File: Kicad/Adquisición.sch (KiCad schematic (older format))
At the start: 28 parts, among them U2 TLC2274, U3 TLC2274

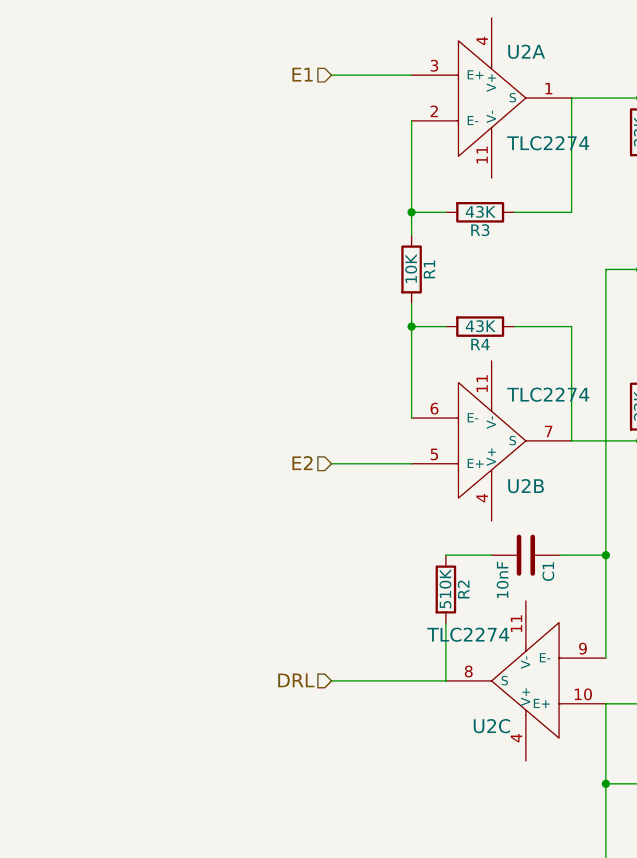
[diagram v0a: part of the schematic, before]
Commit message: Agregados footprints de pin headers para elementos faltantes (falta USB)
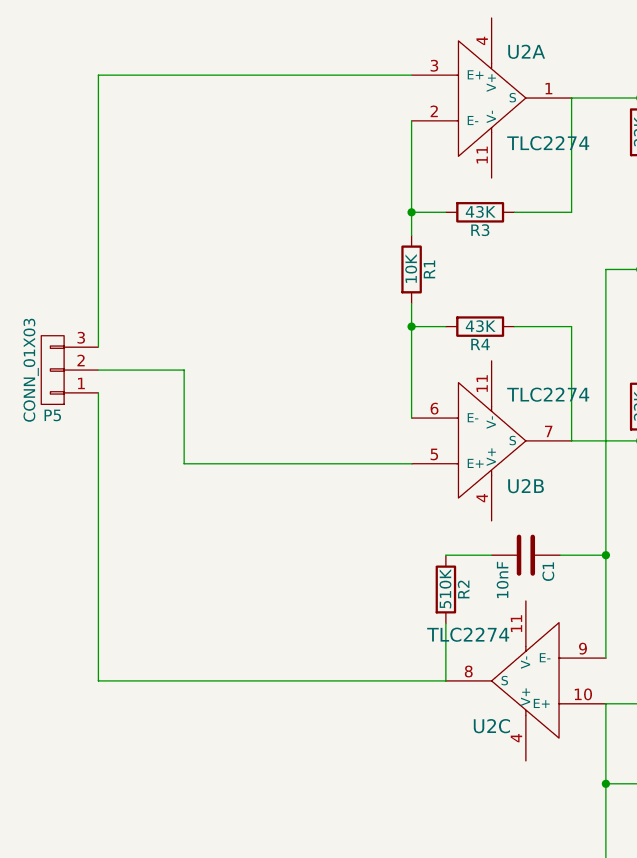
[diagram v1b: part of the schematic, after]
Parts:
- added P5: CONN_01X03, EMG:Pin_Header_Straight_1x03_Pitch2.54mm, symbol CONN_01X03
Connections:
- net DRL: no longer names the net of R2.2, U2.8 (S)
- net DRL: now also P5.1 (P1)
- net E1: no longer names the net of U2.3 (E+)
- net E1: now also P5.3 (P3)
- net E2: no longer names the net of U2.5 (E+)
- net E2: now also P5.2 (P2)
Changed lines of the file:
@@
 $EndComp
 $Comp
-L VCC #PWR1
+L VCC #PWR01
 U 1 1 57DD6A08
 P 4550 5200
-F 0 "#PWR1" H 4550 5050 50  0001 C CNN
+F 0 "#PWR01" H 4550 5050 50  0001 C CNN
 F 1 "VCC" H 4550 5350 50  0000 C CNN
 F 2 "" H 4550 5200 50  0000 C CNN
@@
 $EndComp
 $Comp
-L GND #PWR2
+L GND #PWR02
 U 1 1 57DD6A0E
 P 4550 5900
-F 0 "#PWR2" H 4550 5650 50  0001 C CNN
+F 0 "#PWR02" H 4550 5650 50  0001 C CNN
 F 1 "GND" H 4550 5750 50  0000 C CNN
 F 2 "" H 4550 5900 50  0000 C CNN
@@
 $EndComp
 $Comp
-L GND #PWR7
+L GND #PWR03
 U 1 1 57DD6A14
 P 5750 3700
-F 0 "#PWR7" H 5750 3450 50  0001 C CNN
+F 0 "#PWR03" H 5750 3450 50  0001 C CNN
 F 1 "GND" H 5750 3550 50  0000 C CNN
 F 2 "" H 5750 3700 50  0000 C CNN
@@
 $EndComp
 $Comp
-L VCC #PWR6
+L VCC #PWR04
 U 1 1 57DD6A1A
 P 5750 2800
-F 0 "#PWR6" H 5750 2650 50  0001 C CNN
+F 0 "#PWR04" H 5750 2650 50  0001 C CNN
 F 1 "VCC" H 5750 2950 50  0000 C CNN
 F 2 "" H 5750 2800 50  0000 C CNN
@@
 $EndComp
 $Comp
-L VCC #PWR4
+L VCC #PWR05
 U 1 1 57DD6A3A
 P 5250 5300
-F 0 "#PWR4" H 5250 5150 50  0001 C CNN
+F 0 "#PWR05" H 5250 5150 50  0001 C CNN
 F 1 "VCC" H 5250 5450 50  0000 C CNN
 F 2 "" H 5250 5300 50  0000 C CNN
@@
 $EndComp
 $Comp
-L GND #PWR5
+L GND #PWR06
 U 1 1 57DD6A40
 P 5250 5950
-F 0 "#PWR5" H 5250 5700 50  0001 C CNN
+F 0 "#PWR06" H 5250 5700 50  0001 C CNN
 F 1 "GND" H 5250 5800 50  0000 C CNN
 F 2 "" H 5250 5950 50  0000 C CNN
@@
 $EndComp
 $Comp
-L GND #PWR3
+L GND #PWR07
 U 1 1 57DD6A46
 P 5000 5950
-F 0 "#PWR3" H 5000 5700 50  0001 C CNN
+F 0 "#PWR07" H 5000 5700 50  0001 C CNN
 F 1 "GND" H 5000 5800 50  0000 C CNN
 F 2 "" H 5000 5950 50  0000 C CNN
@@
 Wire Wire Line
 	5250 5650 5250 5600
-Text HLabel 3000 1850 0    60   Input ~ 0
-E1
-Text HLabel 3000 3550 0    60   Input ~ 0
-E2
-Text HLabel 3000 4500 0    60   Input ~ 0
-DRL
-Wire Wire Line
-	3000 3550 3350 3550
-Wire Wire Line
-	3000 1850 3350 1850
 $Comp
 L R R20
@@
 $EndComp
 $Comp
-L GND #PWR8
+L GND #PWR08
 U 1 1 57DD7EDB
 P 8050 3550
-F 0 "#PWR8" H 8050 3300 50  0001 C CNN
+F 0 "#PWR08" H 8050 3300 50  0001 C CNN
 F 1 "GND" H 8050 3400 50  0000 C CNN
 F 2 "" H 8050 3550 50  0000 C CNN
@@
 Vout
 Connection ~ 8050 3250
+$Comp
+L CONN_01X03 P5
+U 1 1 58A72533
+P 1780 3140
+F 0 "P5" H 1780 3340 50  0000 C CNN
+F 1 "CONN_01X03" V 1880 3140 50  0000 C CNN
+F 2 "EMG:Pin_Header_Straight_1x03_Pitch2.54mm" H 1780 3140 50  0001 C CNN
+F 3 "" H 1780 3140 50  0000 C CNN
+	1    1780 3140
+	-1   0    0    1
+$EndComp
 Wire Wire Line
-	3000 4500 3500 4500
+	1980 3240 1980 4500
+Wire Wire Line
+	1980 4500 3500 4500
+Wire Wire Line
+	3350 3550 2355 3550
+Wire Wire Line
+	2355 3550 2355 3140
+Wire Wire Line
+	2355 3140 1980 3140
+Wire Wire Line
+	1980 3040 1980 1850
+Wire Wire Line
+	1980 1850 3350 1850
 $EndSCHEMATC

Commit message: Versión unificada
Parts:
- C1, C2, C3, C4, C5, C6: footprint EMG:C_0805 -> EMG:C_0603
- R1, R10, R11, R12, R13, R14, R15, R16, R17, R18, R19, R2, R20, R3, R4, R5, R6, R7, R8, R9: footprint EMG:R_0805 -> EMG:R_0603
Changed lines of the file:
@@
 F 0 "R3" V 3730 2450 50  0000 C CNN
 F 1 "43K" V 3650 2450 50  0000 C CNN
-F 2 "EMG:R_0805" V 3580 2450 50  0001 C CNN
+F 2 "EMG:R_0603" V 3580 2450 50  0001 C CNN
 F 3 "" H 3650 2450 50  0000 C CNN
 	1    3650 2450
@@
 F 0 "R4" V 3730 2950 50  0000 C CNN
 F 1 "43K" V 3650 2950 50  0000 C CNN
-F 2 "EMG:R_0805" V 3580 2950 50  0001 C CNN
+F 2 "EMG:R_0603" V 3580 2950 50  0001 C CNN
 F 3 "" H 3650 2950 50  0000 C CNN
 	1    3650 2950
@@
 F 0 "R1" V 3430 2700 50  0000 C CNN
 F 1 "10K" V 3350 2700 50  0000 C CNN
-F 2 "EMG:R_0805" V 3280 2700 50  0001 C CNN
+F 2 "EMG:R_0603" V 3280 2700 50  0001 C CNN
 F 3 "" H 3350 2700 50  0000 C CNN
 	1    3350 2700
@@
 F 0 "R5" V 4430 2100 50  0000 C CNN
 F 1 "22K" V 4350 2100 50  0000 C CNN
-F 2 "EMG:R_0805" V 4280 2100 50  0001 C CNN
+F 2 "EMG:R_0603" V 4280 2100 50  0001 C CNN
 F 3 "" H 4350 2100 50  0000 C CNN
 	1    4350 2100
@@
 F 0 "R6" V 4430 3300 50  0000 C CNN
 F 1 "22K" V 4350 3300 50  0000 C CNN
-F 2 "EMG:R_0805" V 4280 3300 50  0001 C CNN
+F 2 "EMG:R_0603" V 4280 3300 50  0001 C CNN
 F 3 "" H 4350 3300 50  0000 C CNN
 	1    4350 3300
@@
 F 0 "R7" V 5080 2100 50  0000 C CNN
 F 1 "10M" V 5000 2100 50  0000 C CNN
-F 2 "EMG:R_0805" V 4930 2100 50  0001 C CNN
+F 2 "EMG:R_0603" V 4930 2100 50  0001 C CNN
 F 3 "" H 5000 2100 50  0000 C CNN
 	1    5000 2100
@@
 F 0 "R8" V 5080 3300 50  0000 C CNN
 F 1 "10M" V 5000 3300 50  0000 C CNN
-F 2 "EMG:R_0805" V 4930 3300 50  0001 C CNN
+F 2 "EMG:R_0603" V 4930 3300 50  0001 C CNN
 F 3 "" H 5000 3300 50  0000 C CNN
 	1    5000 3300
@@
 F 0 "R13" V 5630 2500 50  0000 C CNN
 F 1 "430K" V 5550 2500 50  0000 C CNN
-F 2 "EMG:R_0805" V 5480 2500 50  0001 C CNN
+F 2 "EMG:R_0603" V 5480 2500 50  0001 C CNN
 F 3 "" H 5550 2500 50  0000 C CNN
 	1    5550 2500
@@
 F 0 "R14" V 5630 2900 50  0000 C CNN
 F 1 "430K" V 5550 2900 50  0000 C CNN
-F 2 "EMG:R_0805" V 5480 2900 50  0001 C CNN
+F 2 "EMG:R_0603" V 5480 2900 50  0001 C CNN
 F 3 "" H 5550 2900 50  0000 C CNN
 	1    5550 2900
@@
 F 0 "R12" V 5480 2700 50  0000 C CNN
 F 1 "43K" V 5400 2700 50  0000 C CNN
-F 2 "EMG:R_0805" V 5330 2700 50  0001 C CNN
+F 2 "EMG:R_0603" V 5330 2700 50  0001 C CNN
 F 3 "" H 5400 2700 50  0000 C CNN
 	1    5400 2700
@@
 F 0 "C2" H 4675 2050 50  0000 L CNN
 F 1 "0.33uF" H 4675 1850 50  0000 L CNN
-F 2 "EMG:C_0805" H 4688 1800 50  0001 C CNN
+F 2 "EMG:C_0603" H 4688 1800 50  0001 C CNN
 F 3 "" H 4650 1950 50  0000 C CNN
 	1    4650 1950
@@
 F 0 "C3" H 4675 3550 50  0000 L CNN
 F 1 "0.33uF" H 4675 3350 50  0000 L CNN
-F 2 "EMG:C_0805" H 4688 3300 50  0001 C CNN
+F 2 "EMG:C_0603" H 4688 3300 50  0001 C CNN
 F 3 "" H 4650 3450 50  0000 C CNN
 	1    4650 3450
@@
 F 0 "R15" V 6480 3350 50  0000 C CNN
 F 1 "43K" V 6400 3350 50  0000 C CNN
-F 2 "EMG:R_0805" V 6330 3350 50  0001 C CNN
+F 2 "EMG:R_0603" V 6330 3350 50  0001 C CNN
 F 3 "" H 6400 3350 50  0000 C CNN
 	1    6400 3350
@@
 F 0 "R16" V 6780 2550 50  0000 C CNN
 F 1 "43K" V 6700 2550 50  0000 C CNN
-F 2 "EMG:R_0805" V 6630 2550 50  0001 C CNN
+F 2 "EMG:R_0603" V 6630 2550 50  0001 C CNN
 F 3 "" H 6700 2550 50  0000 C CNN
 	1    6700 2550
@@
 F 0 "R18" V 7080 2700 50  0000 C CNN
 F 1 "215K" V 7000 2700 50  0000 C CNN
-F 2 "EMG:R_0805" V 6930 2700 50  0001 C CNN
+F 2 "EMG:R_0603" V 6930 2700 50  0001 C CNN
 F 3 "" H 7000 2700 50  0000 C CNN
 	1    7000 2700
@@
 F 0 "R17" V 6780 3550 50  0000 C CNN
 F 1 "215K" V 6700 3550 50  0000 C CNN
-F 2 "EMG:R_0805" V 6630 3550 50  0001 C CNN
+F 2 "EMG:R_0603" V 6630 3550 50  0001 C CNN
 F 3 "" H 6700 3550 50  0000 C CNN
 	1    6700 3550
@@
 F 0 "C5" H 6925 3800 50  0000 L CNN
 F 1 "0.68uF" H 6925 3600 50  0000 L CNN
-F 2 "EMG:C_0805" H 6938 3550 50  0001 C CNN
+F 2 "EMG:C_0603" H 6938 3550 50  0001 C CNN
 F 3 "" H 6900 3700 50  0000 C CNN
 	1    6900 3700
@@
 F 0 "R19" V 7330 3700 50  0000 C CNN
 F 1 "10M" V 7250 3700 50  0000 C CNN
-F 2 "EMG:R_0805" V 7180 3700 50  0001 C CNN
+F 2 "EMG:R_0603" V 7180 3700 50  0001 C CNN
 F 3 "" H 7250 3700 50  0000 C CNN
 	1    7250 3700
@@
 F 0 "R9" V 5330 4000 50  0000 C CNN
 F 1 "10M" V 5250 4000 50  0000 C CNN
-F 2 "EMG:R_0805" V 5180 4000 50  0001 C CNN
+F 2 "EMG:R_0603" V 5180 4000 50  0001 C CNN
 F 3 "" H 5250 4000 50  0000 C CNN
 	1    5250 4000
@@
 F 0 "C1" H 3875 4050 50  0000 L CNN
 F 1 "10nF" H 3875 3850 50  0000 L CNN
-F 2 "EMG:C_0805" H 3888 3800 50  0001 C CNN
+F 2 "EMG:C_0603" H 3888 3800 50  0001 C CNN
 F 3 "" H 3850 3950 50  0000 C CNN
 	1    3850 3950
@@
 F 0 "R2" V 3580 4100 50  0000 C CNN
 F 1 "510K" V 3500 4100 50  0000 C CNN
-F 2 "EMG:R_0805" V 3430 4100 50  0001 C CNN
+F 2 "EMG:R_0603" V 3430 4100 50  0001 C CNN
 F 3 "" H 3500 4100 50  0000 C CNN
 	1    3500 4100
@@
 F 0 "C4" H 5025 5900 50  0000 L CNN
 F 1 "1uF" H 5025 5700 50  0000 L CNN
-F 2 "EMG:C_0805" H 5038 5650 50  0001 C CNN
+F 2 "EMG:C_0603" H 5038 5650 50  0001 C CNN
 F 3 "" H 5000 5800 50  0000 C CNN
 	1    5000 5800
@@
 F 0 "R11" V 5330 5800 50  0000 C CNN
 F 1 "1M" V 5250 5800 50  0000 C CNN
-F 2 "EMG:R_0805" V 5180 5800 50  0001 C CNN
+F 2 "EMG:R_0603" V 5180 5800 50  0001 C CNN
 F 3 "" H 5250 5800 50  0000 C CNN
 	1    5250 5800
@@
 F 0 "R10" V 5330 5450 50  0000 C CNN
 F 1 "1M" V 5250 5450 50  0000 C CNN
-F 2 "EMG:R_0805" V 5180 5450 50  0001 C CNN
+F 2 "EMG:R_0603" V 5180 5450 50  0001 C CNN
 F 3 "" H 5250 5450 50  0000 C CNN
 	1    5250 5450
@@
 F 0 "R20" V 7830 3250 50  0000 C CNN
 F 1 "1600K" V 7750 3250 50  0000 C CNN
-F 2 "EMG:R_0805" V 7680 3250 50  0001 C CNN
+F 2 "EMG:R_0603" V 7680 3250 50  0001 C CNN
 F 3 "" H 7750 3250 50  0000 C CNN
 	1    7750 3250
@@
 F 0 "C6" H 8075 3500 50  0000 L CNN
 F 1 "1uF" H 8075 3300 50  0000 L CNN
-F 2 "EMG:C_0805" H 8088 3250 50  0001 C CNN
+F 2 "EMG:C_0603" H 8088 3250 50  0001 C CNN
 F 3 "" H 8050 3400 50  0000 C CNN
 	1    8050 3400

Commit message: Cambios en tamaño de pinheaders
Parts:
- P5: footprint EMG:Pin_Header_Straight_1x03_Pitch2.54mm -> EMG:Pin_Header_Straight_1x03_Pitch1.27mm
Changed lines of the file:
@@
 F 0 "P5" H 1780 3340 50  0000 C CNN
 F 1 "CONN_01X03" V 1880 3140 50  0000 C CNN
-F 2 "EMG:Pin_Header_Straight_1x03_Pitch2.54mm" H 1780 3140 50  0001 C CNN
+F 2 "EMG:Pin_Header_Straight_1x03_Pitch1.27mm" H 1780 3140 50  0001 C CNN
 F 3 "" H 1780 3140 50  0000 C CNN
 	1    1780 3140

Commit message: Se agregaron los 3d shapes de el cargador y dc/dc
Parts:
- U2, U3: footprint EMG:TSSOP-14_4.4x5mm_Pitch0.65mm -> EMG:TSSOP-14
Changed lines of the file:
@@
 F 0 "U2" H 3850 2150 60  0000 C CNN
 F 1 "TLC2274" H 3950 1750 60  0000 C CNN
-F 2 "EMG:TSSOP-14_4.4x5mm_Pitch0.65mm" H 3700 1950 60  0001 C CNN
+F 2 "EMG:TSSOP-14" H 3700 1950 60  0001 C CNN
 F 3 "" H 3700 1950 60  0000 C CNN
 	1    3700 1950
@@
 F 0 "U2" H 3850 3650 60  0000 C CNN
 F 1 "TLC2274" H 3950 3250 60  0000 C CNN
-F 2 "EMG:TSSOP-14_4.4x5mm_Pitch0.65mm" H 3700 3450 60  0001 C CNN
+F 2 "EMG:TSSOP-14" H 3700 3450 60  0001 C CNN
 F 3 "" H 3700 3450 60  0000 C CNN
 	2    3700 3450
@@
 F 0 "U3" H 5900 2250 60  0000 C CNN
 F 1 "TLC2274" H 6000 1850 60  0000 C CNN
-F 2 "EMG:TSSOP-14_4.4x5mm_Pitch0.65mm" H 5750 2050 60  0001 C CNN
+F 2 "EMG:TSSOP-14" H 5750 2050 60  0001 C CNN
 F 3 "" H 5750 2050 60  0000 C CNN
 	1    5750 2050
@@
 F 0 "U3" H 5900 3550 60  0000 C CNN
 F 1 "TLC2274" H 6000 3150 60  0000 C CNN
-F 2 "EMG:TSSOP-14_4.4x5mm_Pitch0.65mm" H 5750 3350 60  0001 C CNN
+F 2 "EMG:TSSOP-14" H 5750 3350 60  0001 C CNN
 F 3 "" H 5750 3350 60  0000 C CNN
 	2    5750 3350
@@
 F 0 "U3" H 7200 3450 60  0000 C CNN
 F 1 "TLC2274" H 7300 3050 60  0000 C CNN
-F 2 "EMG:TSSOP-14_4.4x5mm_Pitch0.65mm" H 7050 3250 60  0001 C CNN
+F 2 "EMG:TSSOP-14" H 7050 3250 60  0001 C CNN
 F 3 "" H 7050 3250 60  0000 C CNN
 	4    7050 3250
@@
 F 0 "U3" H 6850 4400 60  0000 C CNN
 F 1 "TLC2274" H 6950 4000 60  0000 C CNN
-F 2 "EMG:TSSOP-14_4.4x5mm_Pitch0.65mm" H 6700 4200 60  0001 C CNN
+F 2 "EMG:TSSOP-14" H 6700 4200 60  0001 C CNN
 F 3 "" H 6700 4200 60  0000 C CNN
 	3    6700 4200
@@
 F 0 "U2" H 4000 4700 60  0000 C CNN
 F 1 "TLC2274" H 4100 4300 60  0000 C CNN
-F 2 "EMG:TSSOP-14_4.4x5mm_Pitch0.65mm" H 3850 4500 60  0001 C CNN
+F 2 "EMG:TSSOP-14" H 3850 4500 60  0001 C CNN
 F 3 "" H 3850 4500 60  0000 C CNN
 	3    3850 4500
@@
 F 0 "U2" H 4700 5750 60  0000 C CNN
 F 1 "TLC2274" H 4800 5350 60  0000 C CNN
-F 2 "EMG:TSSOP-14_4.4x5mm_Pitch0.65mm" H 4550 5550 60  0001 C CNN
+F 2 "EMG:TSSOP-14" H 4550 5550 60  0001 C CNN
 F 3 "" H 4550 5550 60  0000 C CNN
 	4    4550 5550
